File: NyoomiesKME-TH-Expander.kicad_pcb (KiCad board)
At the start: 2 copper layers, 33.8 x 14 mm, 13 parts, among them J1 2x4 Dupont Socket, J2 JST XH 2 Pin, J3 JST XH 2 Pin, J4 JST XH 2 Pin, J5 JST XH 2 Pin

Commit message: rename to TH Expander
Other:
- board text added: "NyoomiesKME TH Expander"
- board text removed: "NyoomiesKME NTC Expander"
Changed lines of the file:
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@@
 	)
 	(gr_text "HW Rev 0.2"
-		(at 149.5 97.5 0)
+		(at 141.5 101.25 90)
 		(layer "B.SilkS")
 		(effects
@@
 		)
 	)
-	(gr_text "NyoomiesKME\nNTC Expander"
-		(at 155 96 90)
+	(gr_text "NyoomiesKME\nTH Expander"
+		(at 156 96 90)
 		(layer "B.SilkS")
 		(effects

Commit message: add sheet info to pcb doc
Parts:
- moved C1 4.51 mm to (147.0, 98.2)
- moved C2 4.51 mm to (160.8, 98.2)
- moved C3 4.51 mm to (147.0, 104.5)
- moved C4 4.51 mm to (160.8, 104.5)
- moved J1 4.51 mm to (150.2, 103.3)
- moved J2 4.51 mm to (140.0, 97.2)
- moved J3 4.51 mm to (165.2, 97.2)
- moved J4 4.51 mm to (142.5, 105.3)
- moved J5 4.51 mm to (167.8, 105.2)
- moved R1 4.51 mm to (151.5, 98.0)
- moved R2 4.51 mm to (156.5, 98.0)
- moved R3 4.51 mm to (151.5, 105.5)
- moved R4 4.51 mm to (156.5, 105.5)

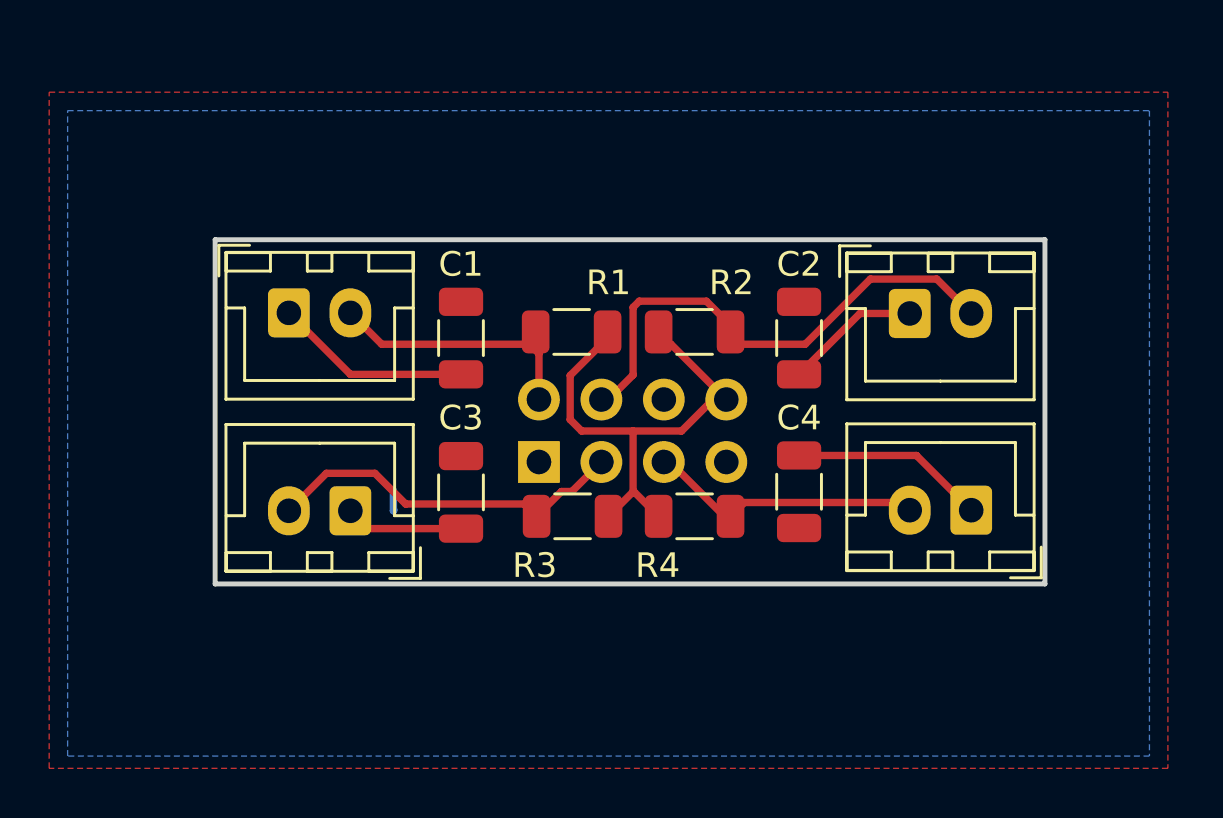
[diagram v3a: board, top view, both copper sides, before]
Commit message: use filtering caps correctly and use labels instead of global labels
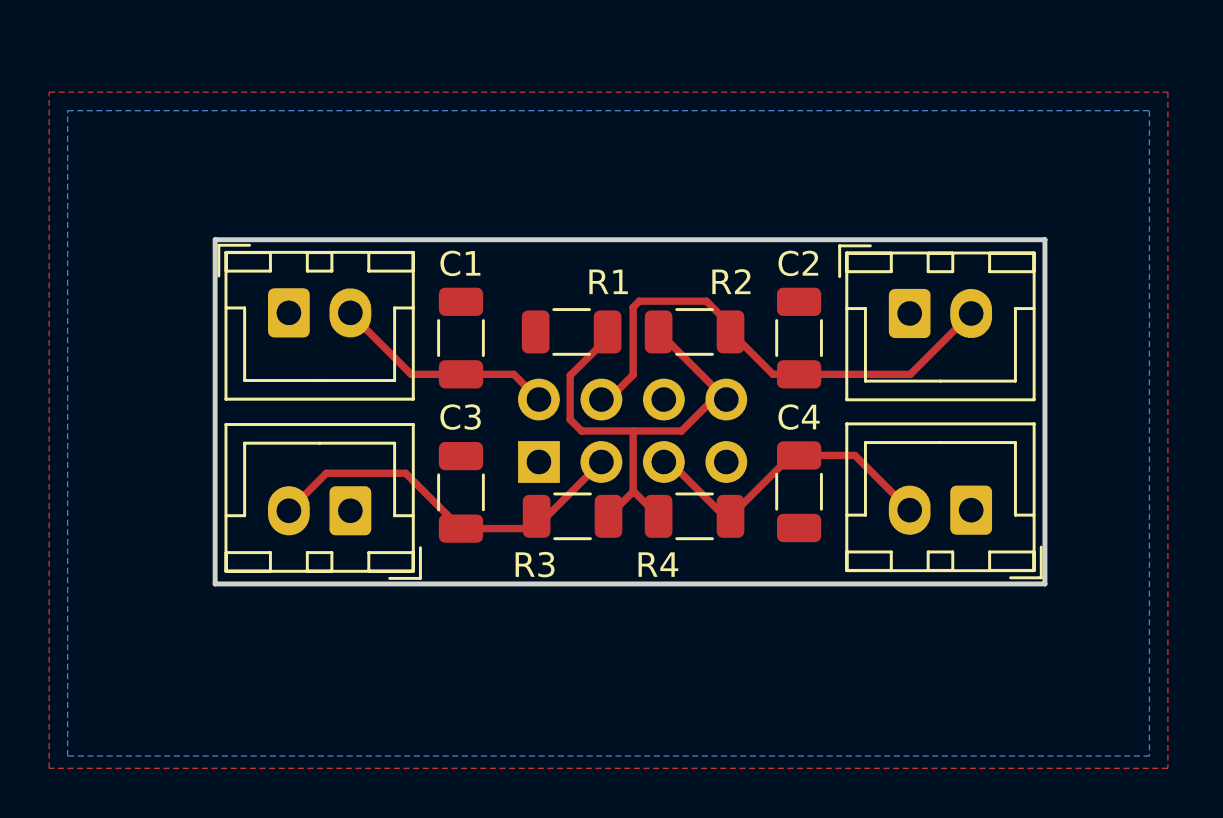
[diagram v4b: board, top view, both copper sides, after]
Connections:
- C1 pad 1: Net-(J2-Pin_1) -> /A1
- C2 pad 1: Net-(J3-Pin_1) -> /A2
- C3 pad 1: Net-(J4-Pin_1) -> /A3
- C4 pad 1: Net-(J5-Pin_1) -> /A4
- J1 pad 2: A1 -> /A1
- J1 pad 3: A3 -> /A3
- J1 pad 4: A2 -> /A2
- J1 pad 5: A4 -> /A4
- J2 pad 1: Net-(J2-Pin_1) -> GND
- J2 pad 2: A1 -> /A1
- J3 pad 1: Net-(J3-Pin_1) -> GND
- J3 pad 2: A2 -> /A2
- J4 pad 1: Net-(J4-Pin_1) -> GND
- J4 pad 2: A3 -> /A3
- J5 pad 1: Net-(J5-Pin_1) -> GND
- J5 pad 2: A4 -> /A4
- R1 pad 1: A1 -> /A1
- R2 pad 1: A2 -> /A2
- R3 pad 1: A3 -> /A3
- R4 pad 1: A4 -> /A4
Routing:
- net /A2: track 0.00 -> 21.7 mm
- net A2: track 21.7 -> 0.00 mm
- net /A3: track 0.00 -> 16.2 mm
- net A3: track 15.8 -> 0.00 mm
- net /A4: track 0.00 -> 13.3 mm
- net A4: track 11.8 -> 0.00 mm
- net A1: track 10.3 -> 0.00 mm
- net /A1: track 0.00 -> 9.22 mm
- net Net-(J2-Pin_1): track 8.04 -> 0.00 mm
- net Net-(J5-Pin_1): track 7.92 -> 0.00 mm
- net Net-(J3-Pin_1): track 5.53 -> 0.00 mm
- net Net-(J4-Pin_1): track 4.84 -> 0.00 mm
- net GND: track 0.86 -> 0.04 mm

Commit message: minor routing improvements
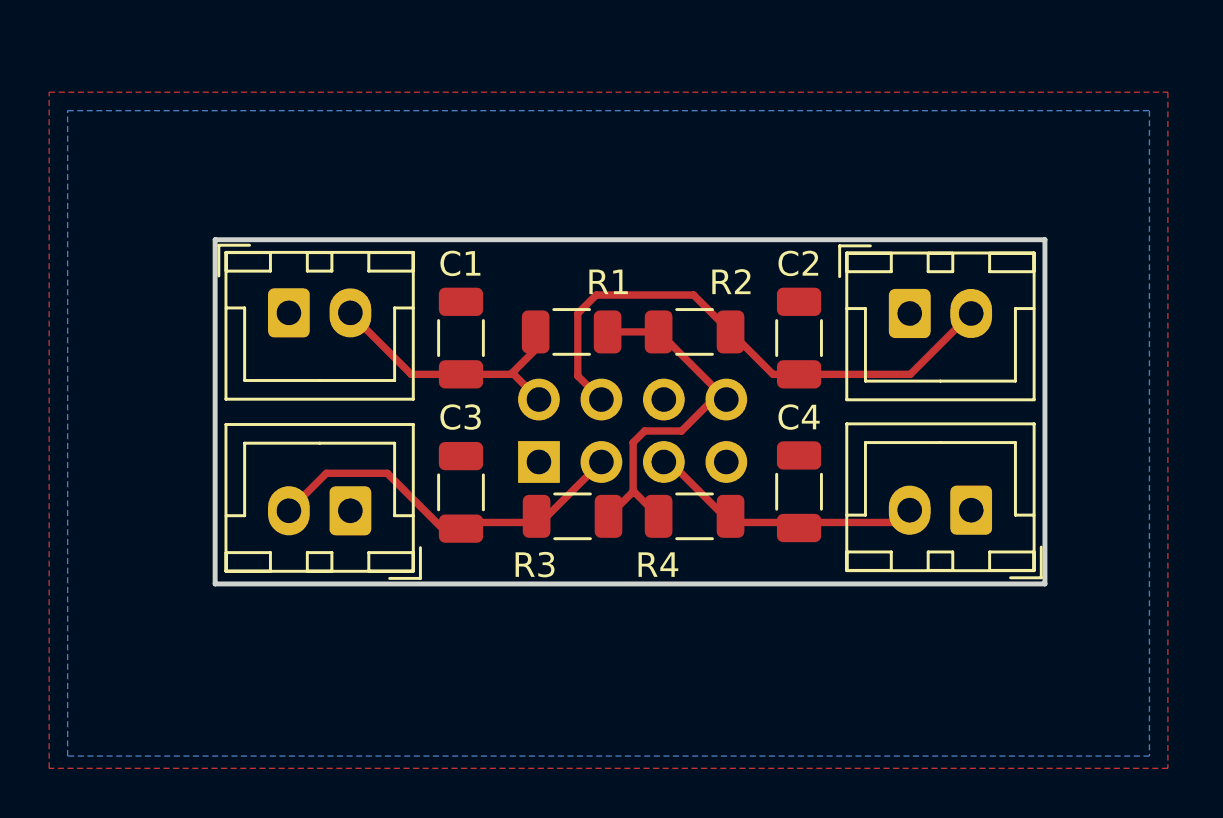
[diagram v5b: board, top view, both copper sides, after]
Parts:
- turned C4 to 90 degrees
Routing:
- net +3.3V: track 19.7 -> 15.1 mm
- net /A1: track 9.22 -> 11.4 mm
- net /A4: track 13.3 -> 11.9 mm
- net /A2: track 21.7 -> 23.1 mm

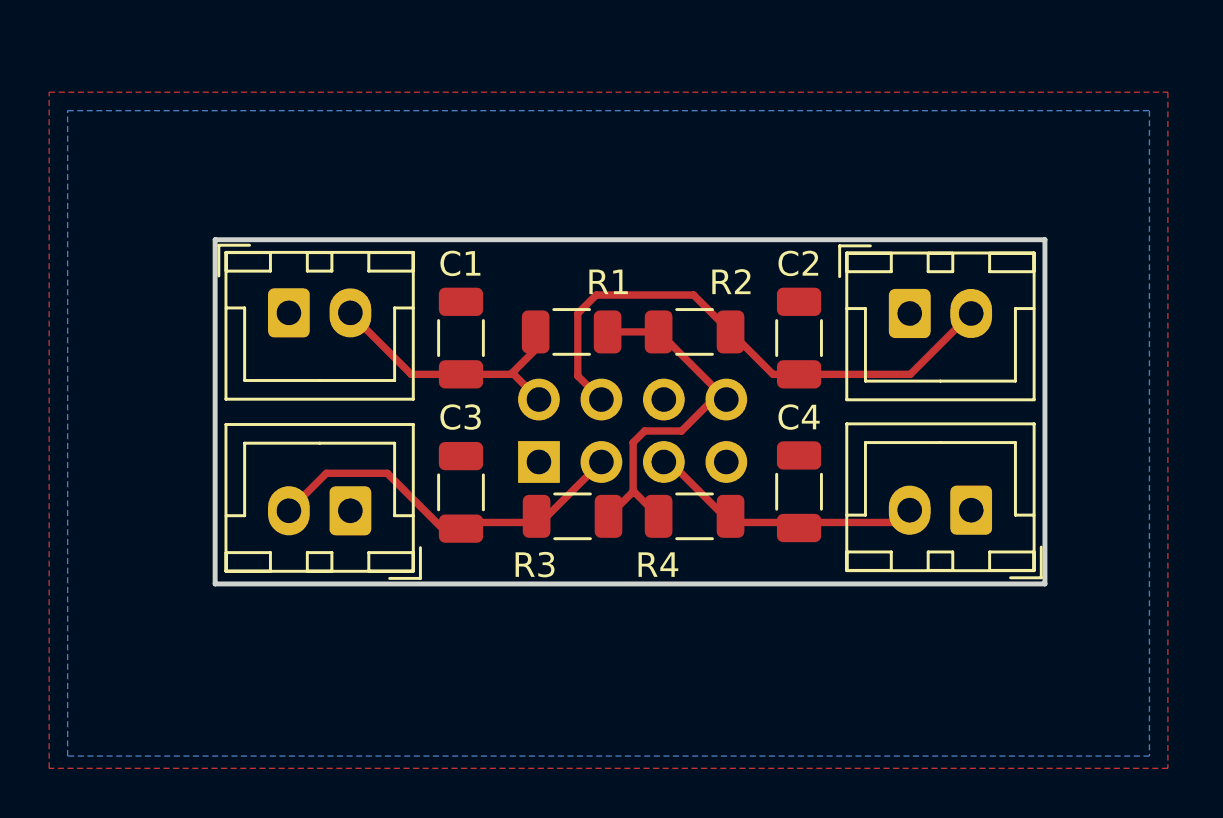
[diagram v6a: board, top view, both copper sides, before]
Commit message: rev 0.3 - change header position, improve silkscreen
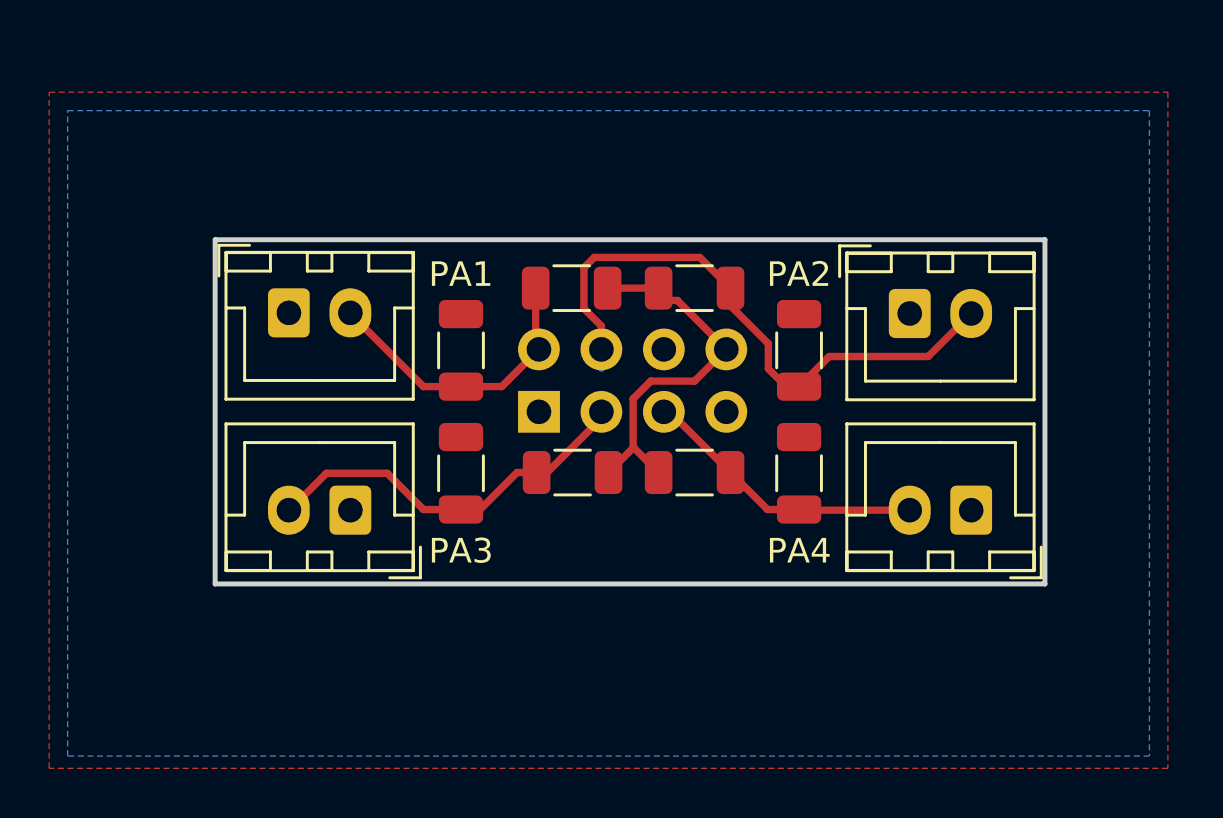
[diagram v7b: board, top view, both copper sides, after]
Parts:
- moved J1 2.04 mm to (150.2, 101.2)
- moved R1 1.78 mm to (151.5, 96.2)
- moved R2 1.78 mm to (156.5, 96.2)
- moved R3 1.78 mm to (151.5, 103.7)
- moved R4 1.78 mm to (156.5, 103.7)
- moved C3 0.78 mm to (147.0, 103.8)
- moved C4 0.75 mm to (160.8, 103.8)
- moved C1 0.50 mm to (147.0, 98.8)
- moved C2 0.50 mm to (160.8, 98.8)
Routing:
- net /A2: track 23.1 -> 24.7 mm
- net /A1: track 11.4 -> 12.4 mm
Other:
- board text added: "HW Rev 0.3"
- board text added: "github.com/PhilippMolitor"
- board text removed: "HW Rev 0.2"
- board text removed: "github.com/ PhilippMolitor"
